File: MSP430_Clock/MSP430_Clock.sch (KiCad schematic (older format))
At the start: 0 parts

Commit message: Add LCD Display to Schematic
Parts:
- added DS?: LCD16X2, WC1602A, symbol LCD16X2
- added U?: MSP430G2553IN20, symbol MSP430G2553IN20
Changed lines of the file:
@@
 LIBS:contrib
 LIBS:valves
+LIBS:embedded-microcontrollers
+LIBS:MSP430_Clock-cache
 EELAYER 25 0
 EELAYER END
@@
 Comment4 ""
 $EndDescr
+$Comp
+L MSP430G2553IN20 U?
+U 1 1 58FAC7AC
+P 4700 2300
+F 0 "U?" H 7150 2400 60  0000 C CNN
+F 1 "MSP430G2553IN20" H 6000 1000 60  0000 C CNN
+F 2 "" H 4700 2300 60  0000 C CNN
+F 3 "" H 4700 2300 60  0000 C CNN
+	1    4700 2300
+	1    0    0    -1
+$EndComp
+$Comp
+L +12V #PWR?
+U 1 1 58FAC7FC
+P 10550 850
+F 0 "#PWR?" H 10550 700 50  0001 C CNN
+F 1 "+12V" H 10550 990 50  0000 C CNN
+F 2 "" H 10550 850 50  0000 C CNN
+F 3 "" H 10550 850 50  0000 C CNN
+	1    10550 850
+	1    0    0    -1
+$EndComp
+$Comp
+L GND #PWR?
+U 1 1 58FAC815
+P 10550 5900
+F 0 "#PWR?" H 10550 5650 50  0001 C CNN
+F 1 "GND" H 10550 5750 50  0000 C CNN
+F 2 "" H 10550 5900 50  0000 C CNN
+F 3 "" H 10550 5900 50  0000 C CNN
+	1    10550 5900
+	1    0    0    -1
+$EndComp
+$Comp
+L LCD16X2 DS?
+U 1 1 58FACB94
+P 2250 1700
+F 0 "DS?" H 1450 2100 50  0000 C CNN
+F 1 "LCD16X2" H 2950 2100 50  0000 C CNN
+F 2 "WC1602A" H 2250 1650 50  0000 C CIN
+F 3 "" H 2250 1700 50  0000 C CNN
+	1    2250 1700
+	1    0    0    -1
+$EndComp
 $EndSCHEMATC

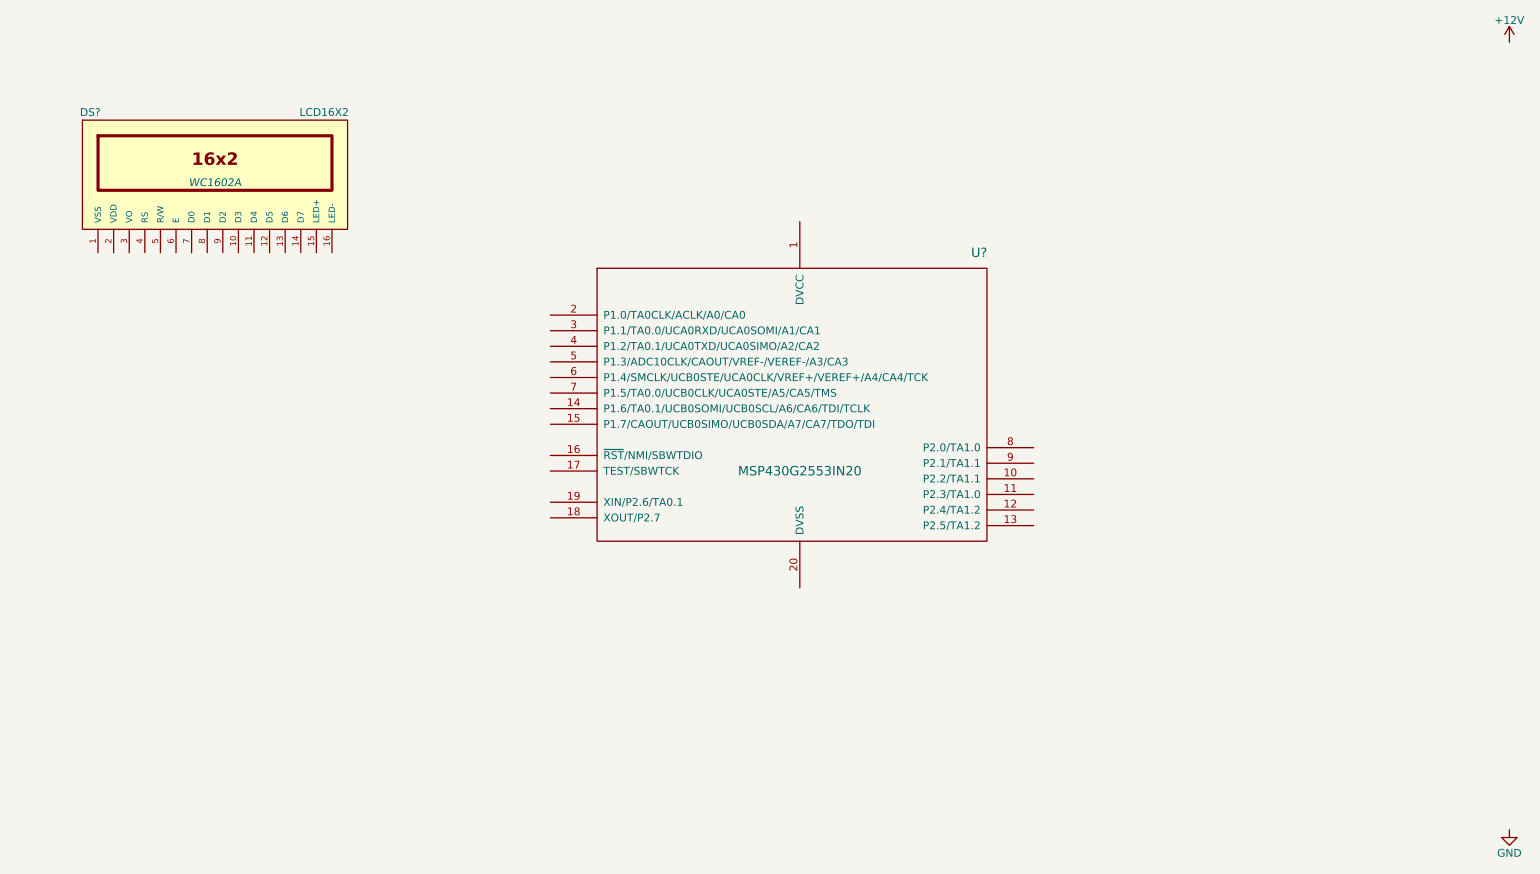
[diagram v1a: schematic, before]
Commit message: Add power and ground nodes to schematic
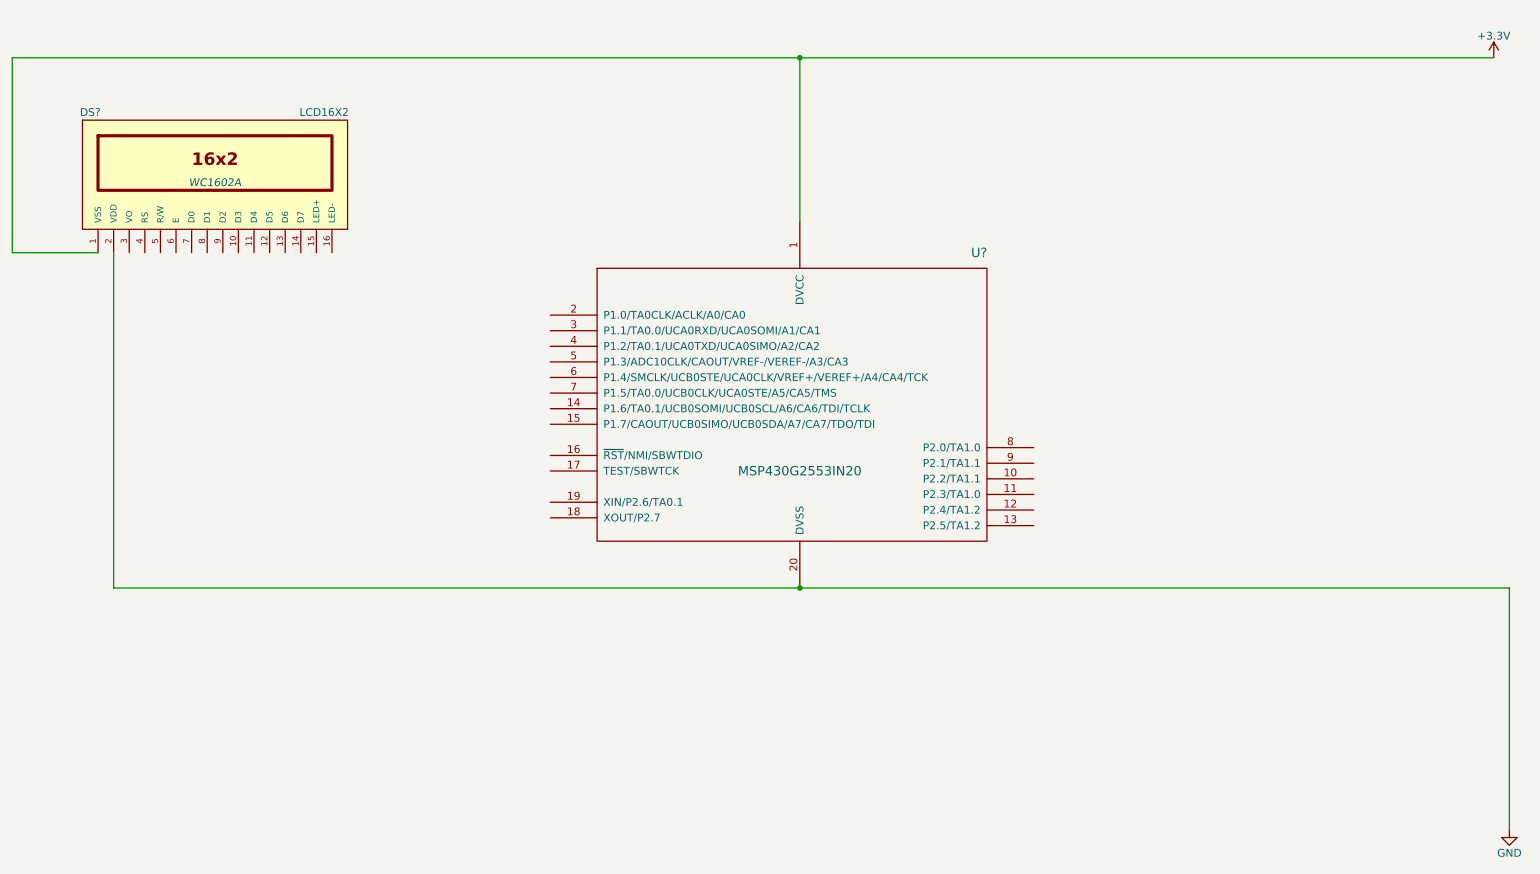
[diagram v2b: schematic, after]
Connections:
- net GND: now also DS?.2 (VDD), U?.20 (DVSS)
- net +3V3: now reaches U?.1 (DVCC)
- net +3V3: now also DS?.1 (VSS)
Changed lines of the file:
@@
-$EndComp
-$Comp
-L +12V #PWR?
-U 1 1 58FAC7FC
-P 10550 850
-F 0 "#PWR?" H 10550 700 50  0001 C CNN
-F 1 "+12V" H 10550 990 50  0000 C CNN
-F 2 "" H 10550 850 50  0000 C CNN
-F 3 "" H 10550 850 50  0000 C CNN
-	1    10550 850
-	1    0    0    -1
 $EndComp
 $Comp
@@
 	1    0    0    -1
 $EndComp
+$Comp
+L +3.3V #PWR?
+U 1 1 58FACE99
+P 10450 950
+F 0 "#PWR?" H 10450 800 50  0001 C CNN
+F 1 "+3.3V" H 10450 1090 50  0000 C CNN
+F 2 "" H 10450 950 50  0000 C CNN
+F 3 "" H 10450 950 50  0000 C CNN
+	1    10450 950
+	1    0    0    -1
+$EndComp
+Wire Wire Line
+	950  950  10450 950
+Wire Wire Line
+	6000 950  6000 2000
+Wire Wire Line
+	1500 2200 950  2200
+Wire Wire Line
+	950  2200 950  950
+Connection ~ 6000 950
+Wire Wire Line
+	1600 4350 10550 4350
+Wire Wire Line
+	10550 4350 10550 5900
+Wire Wire Line
+	1600 2200 1600 4350
+Connection ~ 6000 4350
 $EndSCHEMATC
